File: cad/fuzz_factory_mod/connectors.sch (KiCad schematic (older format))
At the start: 21 parts, among them J1701 Barrel_Jack_Switch, J1702 Conn_Battery, J1703 CONN_AUDIO_IN, J1704 CONN_AUDIO_OUT, J2801 CONN_AUDIO_OUT_REF, J2802 CONN_EXP_1, J2803 CONN_EXP_2, K1701 EE2-5NU, Q1701 DTC114Y, Q1702 DTA114E

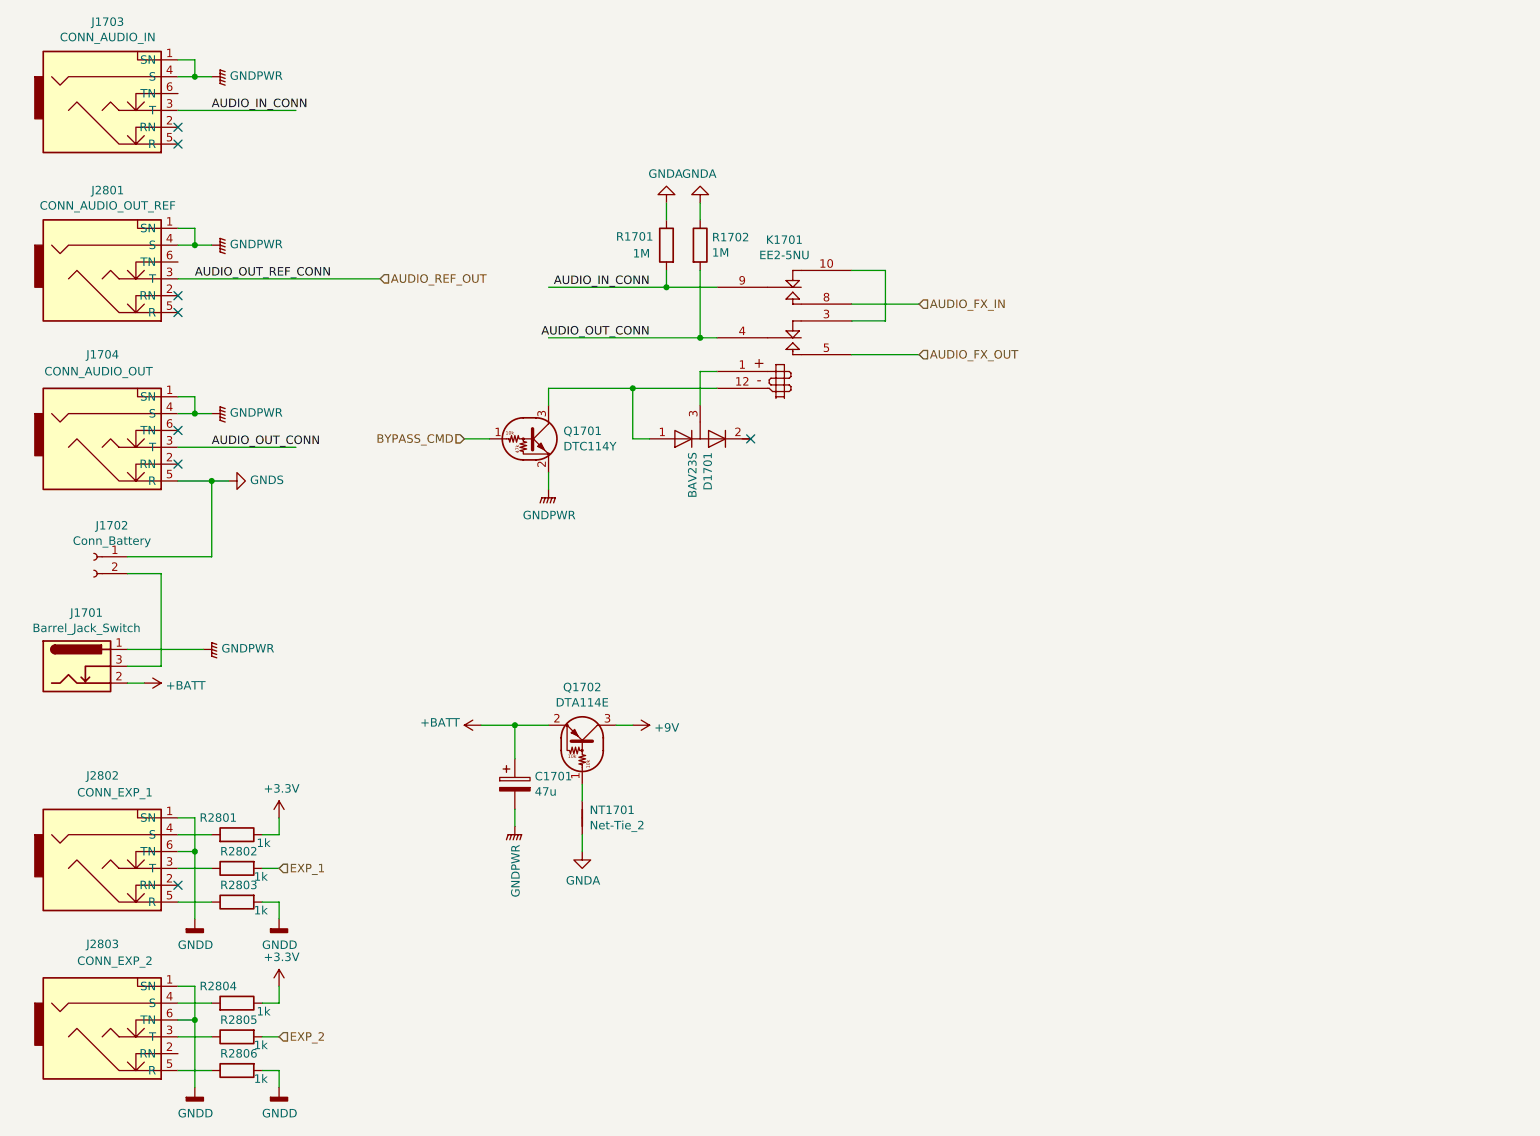
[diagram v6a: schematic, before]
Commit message: Changes architecture.
Corrections on schematic.
Continued Layout placement.
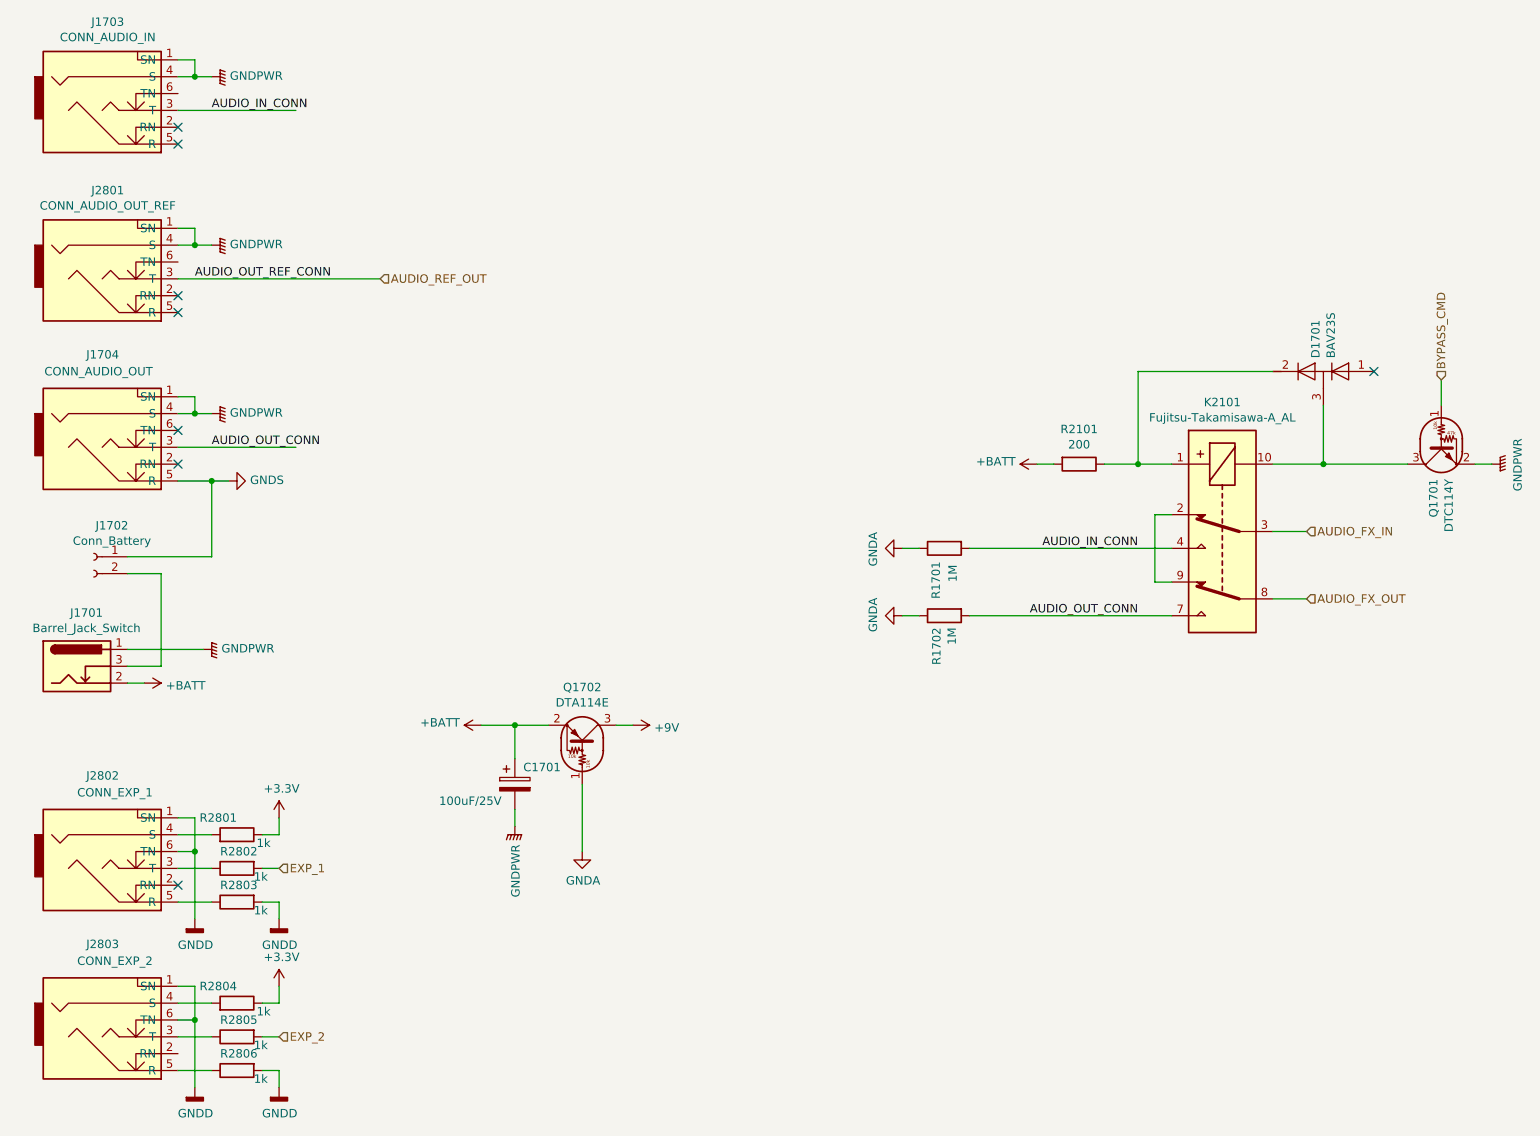
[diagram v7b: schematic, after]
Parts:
- removed K1701: EE2-5NU, flax_lib:RELAY-EE2, symbol flax_lib:EE2-5NU
- removed NT1701: Net-Tie_2, Oddities:NetTie-II, symbol Device:Net-Tie_2
- added K2101: Fujitsu-Takamisawa-A_AL, Relays_ThroughHole:Relay_DPDT_FRT5, symbol flax_lib:Fujitsu-Takamisawa-A_AL
- added R2101: 200, Resistors_SMD:R_0805, symbol Device:R
- C1701: value 47u -> 100uF/25V
- J1703, J1704, J2801, J2802, J2803: footprint Connect:NMJ6HCD2 -> flax_lib:CLIFF_FCR5005x
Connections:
- wire segments 77 -> 73
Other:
- moved on the sheet: D1701, Q1701, R1701, R1702
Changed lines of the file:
@@
 $Descr A4 11693 8268
 encoding utf-8
-Sheet 29 30
+Sheet 21 22
 Title ""
 Date ""
@@
 $EndDescr
 $Comp
-L flax_lib:EE2-5NU K1701
-U 1 1 5DE5A46A
-P 6400 2650
-F 0 "K1701" H 6400 3181 50  0000 C CNN
-F 1 "EE2-5NU" H 6400 3090 50  0000 C CNN
-F 2 "flax_lib:RELAY-EE2" H 6400 2650 50  0001 C CNN
-F 3 "" H 6400 2650 50  0000 C CNN
-	1    6400 2650
-	1    0    0    -1
-$EndComp
-$Comp
 L flax_lib:CLIFF_FCR50051 J1703
 U 1 1 5DE5BD43
@@
 F 0 "J1703" H 2383 1875 50  0000 C CNN
 F 1 "CONN_AUDIO_IN" H 2383 1784 50  0000 C CNN
-F 2 "Connect:NMJ6HCD2" H 2500 1200 50  0001 C CNN
+F 2 "flax_lib:CLIFF_FCR5005x" H 2500 1200 50  0001 C CNN
 F 3 "" H 2500 1200 50  0001 C CNN
 	1    2400 1350
@@
 F 0 "J1704" H 2450 3900 50  0000 R CNN
 F 1 "CONN_AUDIO_OUT" H 2650 3800 50  0000 R CNN
-F 2 "Connect:NMJ6HCD2" H 2500 3200 50  0001 C CNN
+F 2 "flax_lib:CLIFF_FCR5005x" H 2500 3200 50  0001 C CNN
 F 3 "" H 2500 3200 50  0001 C CNN
 	1    2400 3350
@@
 L Transistor_BJT:DTC114Y Q1701
 U 1 1 5DE5E2B7
-P 4900 3300
-F 0 "Q1701" H 5088 3346 50  0000 L CNN
-F 1 "DTC114Y" H 5088 3255 50  0000 L CNN
-F 2 "TO_SOT_Packages_SMD:SOT-23" H 4900 3300 50  0001 L CNN
-F 3 "" H 4900 3300 50  0001 L CNN
-	1    4900 3300
-	1    0    0    -1
+P 10300 3350
+F 0 "Q1701" H 10488 3396 50  0000 L CNN
+F 1 "DTC114Y" H 10488 3305 50  0000 L CNN
+F 2 "TO_SOT_Packages_SMD:SOT-23" H 10300 3350 50  0001 L CNN
+F 3 "" H 10300 3350 50  0001 L CNN
+	1    10300 3350
+	0    -1   1    0
 $EndComp
 $Comp
 L flax_lib:BAV23S D1701
 U 1 1 5DE5F68B
-P 5900 3300
-F 0 "D1701" V 5946 3379 50  0000 L CNN
-F 1 "BAV23S" V 5855 3379 50  0000 L CNN
-F 2 "TO_SOT_Packages_SMD:SOT-23" H 5900 3300 50  0001 C CNN
-F 3 "" H 5900 3300 50  0001 C CNN
-	1    5900 3300
-	1    0    0    1
+P 9600 2900
+F 0 "D1701" V 9646 2979 50  0000 L CNN
+F 1 "BAV23S" V 9555 2979 50  0000 L CNN
+F 2 "TO_SOT_Packages_SMD:SOT-23" H 9600 2900 50  0001 C CNN
+F 3 "" H 9600 2900 50  0001 C CNN
+	1    9600 2900
+	-1   0    0    -1
 $EndComp
 $Comp
@@
 	1    0    0    -1
 $EndComp
-Wire Wire Line
-	6800 2600 7000 2600
-Wire Wire Line
-	7000 2600 7000 2300
-Wire Wire Line
-	7000 2300 6800 2300
 $Comp
 L power:GNDPWR #PWR01706
 U 1 1 5E049671
-P 5000 3600
-F 0 "#PWR01706" H 5000 3400 50  0001 C CNN
-F 1 "GNDPWR" H 5004 3446 50  0000 C CNN
-F 2 "" H 5000 3550 50  0001 C CNN
-F 3 "" H 5000 3550 50  0001 C CNN
-	1    5000 3600
-	1    0    0    -1
-$EndComp
-Wire Wire Line
-	5000 3500 5000 3600
-Wire Wire Line
-	5000 3000 5000 3100
-Wire Wire Line
-	5000 3000 5500 3000
-Wire Wire Line
-	6000 2900 5900 2900
-Wire Wire Line
-	5900 2900 5900 3100
-Wire Wire Line
-	5600 3300 5500 3300
-Wire Wire Line
-	5500 3300 5500 3000
-Connection ~ 5500 3000
-Wire Wire Line
-	5500 3000 6000 3000
-NoConn ~ 6200 3300
-Text HLabel 4500 3300 0    50   Input ~ 0
+P 10600 3450
+F 0 "#PWR01706" H 10600 3250 50  0001 C CNN
+F 1 "GNDPWR" H 10604 3296 50  0000 C CNN
+F 2 "" H 10600 3400 50  0001 C CNN
+F 3 "" H 10600 3400 50  0001 C CNN
+	1    10600 3450
+	0    -1   1    0
+$EndComp
+Wire Wire Line
+	10500 3450 10600 3450
+Text HLabel 10300 2950 1    50   Input ~ 0
 BYPASS_CMD
 Wire Wire Line
-	4650 3300 4500 3300
+	10300 3100 10300 2950
 $Comp
 L Device:R R1702
 U 1 1 5E0563EF
-P 5900 2150
-F 0 "R1702" H 5970 2196 50  0000 L CNN
-F 1 "1M" H 5970 2105 50  0000 L CNN
-F 2 "Resistors_SMD:R_0603" V 5830 2150 50  0001 C CNN
-F 3 "~" H 5900 2150 50  0001 C CNN
-	1    5900 2150
-	1    0    0    -1
+P 7350 4350
+F 0 "R1702" H 7420 4396 50  0000 L CNN
+F 1 "1M" H 7420 4305 50  0000 L CNN
+F 2 "Resistors_SMD:R_0603" V 7280 4350 50  0001 C CNN
+F 3 "~" H 7350 4350 50  0001 C CNN
+	1    7350 4350
+	0    -1   1    0
 $EndComp
 $Comp
 L Device:R R1701
 U 1 1 5E056DB3
-P 5700 2150
-F 0 "R1701" H 6000 2200 50  0000 R CNN
-F 1 "1M" H 5900 2100 50  0000 R CNN
-F 2 "Resistors_SMD:R_0603" V 5630 2150 50  0001 C CNN
-F 3 "~" H 5700 2150 50  0001 C CNN
-	1    5700 2150
-	-1   0    0    -1
-$EndComp
-Wire Wire Line
-	5900 2300 5900 2700
-Connection ~ 5900 2700
-Wire Wire Line
-	5900 2700 6000 2700
-Wire Wire Line
-	5700 2300 5700 2400
-Connection ~ 5700 2400
-Wire Wire Line
-	5700 2400 6000 2400
+P 7350 3950
+F 0 "R1701" H 7650 4000 50  0000 R CNN
+F 1 "1M" H 7550 3900 50  0000 R CNN
+F 2 "Resistors_SMD:R_0603" V 7280 3950 50  0001 C CNN
+F 3 "~" H 7350 3950 50  0001 C CNN
+	1    7350 3950
+	0    -1   1    0
+$EndComp
 $Comp
 L power:GNDA #PWR01710
 U 1 1 5E058766
-P 5900 1900
-F 0 "#PWR01710" H 5900 1650 50  0001 C CNN
-F 1 "GNDA" H 5905 1727 50  0000 C CNN
-F 2 "" H 5900 1900 50  0001 C CNN
-F 3 "" H 5900 1900 50  0001 C CNN
-	1    5900 1900
-	-1   0    0    1
+P 7100 4350
+F 0 "#PWR01710" H 7100 4100 50  0001 C CNN
+F 1 "GNDA" H 7105 4177 50  0000 C CNN
+F 2 "" H 7100 4350 50  0001 C CNN
+F 3 "" H 7100 4350 50  0001 C CNN
+	1    7100 4350
+	0    1    -1   0
 $EndComp
 $Comp
 L power:GNDA #PWR01709
 U 1 1 5E059243
-P 5700 1900
-F 0 "#PWR01709" H 5700 1650 50  0001 C CNN
-F 1 "GNDA" H 5705 1727 50  0000 C CNN
-F 2 "" H 5700 1900 50  0001 C CNN
-F 3 "" H 5700 1900 50  0001 C CNN
-	1    5700 1900
-	-1   0    0    1
-$EndComp
-Wire Wire Line
-	5900 1900 5900 2000
-Wire Wire Line
-	5700 1900 5700 2000
-Text HLabel 7200 2500 2    50   Input ~ 0
+P 7100 3950
+F 0 "#PWR01709" H 7100 3700 50  0001 C CNN
+F 1 "GNDA" H 7105 3777 50  0000 C CNN
+F 2 "" H 7100 3950 50  0001 C CNN
+F 3 "" H 7100 3950 50  0001 C CNN
+	1    7100 3950
+	0    1    1    0
+$EndComp
+Wire Wire Line
+	7100 4350 7200 4350
+Wire Wire Line
+	7100 3950 7200 3950
+Text HLabel 9500 3850 2    50   Input ~ 0
 AUDIO_FX_IN
-Text HLabel 7200 2800 2    50   Input ~ 0
+Text HLabel 9500 4250 2    50   Input ~ 0
 AUDIO_FX_OUT
-Wire Wire Line
-	7200 2800 6800 2800
-Wire Wire Line
-	6800 2500 7200 2500
 Wire Wire Line
 	2600 4750 2500 4750
@@
 NoConn ~ 2800 1450
 NoConn ~ 2800 1550
-Text Label 5600 2400 2    50   ~ 0
+Text Label 8500 3950 2    50   ~ 0
 AUDIO_IN_CONN
-Text Label 5600 2700 2    50   ~ 0
+Text Label 8500 4350 2    50   ~ 0
 AUDIO_OUT_CONN
-Wire Wire Line
-	5000 2700 5900 2700
-Wire Wire Line
-	5000 2400 5700 2400
 $Comp
 L Transistor_BJT:DTA114E Q1702
@@
 	0    1    -1   0
 $EndComp
-$Comp
-L Device:CP C1701
-U 1 1 5E6D0A71
-P 4800 5350
-F 0 "C1701" H 4918 5396 50  0000 L CNN
-F 1 "47u" H 4918 5305 50  0000 L CNN
-F 2 "Capacitors_SMD:CP_Elec_6.3x4.5" H 4838 5200 50  0001 C CNN
-F 3 "~" H 4800 5350 50  0001 C CNN
-	1    4800 5350
-	1    0    0    -1
-$EndComp
 Wire Wire Line
 	5000 5000 4800 5000
@@
 	5500 5000 5400 5000
 $Comp
-L Device:Net-Tie_2 NT1701
-U 1 1 5E6DBA2F
-P 5200 5550
-F 0 "NT1701" V 5154 5594 50  0000 L CNN
-F 1 "Net-Tie_2" V 5245 5594 50  0000 L CNN
-F 2 "Oddities:NetTie-II" H 5200 5550 50  0001 C CNN
-F 3 "~" H 5200 5550 50  0001 C CNN
-	1    5200 5550
-	0    1    1    0
-$EndComp
-Wire Wire Line
-	5200 5350 5200 5450
-Wire Wire Line
-	5200 5650 5200 5750
-$Comp
 L flax_lib:CLIFF_FCR50051 J2802
 U 1 1 5ECDD75B
@@
 F 0 "J2802" H 2450 6400 50  0000 R CNN
 F 1 "CONN_EXP_1" H 2650 6300 50  0000 R CNN
-F 2 "Connect:NMJ6HCD2" H 2500 5700 50  0001 C CNN
+F 2 "flax_lib:CLIFF_FCR5005x" H 2500 5700 50  0001 C CNN
 F 3 "" H 2500 5700 50  0001 C CNN
 	1    2400 5850
@@
 F 0 "J2803" H 2450 7400 50  0000 R CNN
 F 1 "CONN_EXP_2" H 2650 7300 50  0000 R CNN
-F 2 "Connect:NMJ6HCD2" H 2500 6700 50  0001 C CNN
+F 2 "flax_lib:CLIFF_FCR5005x" H 2500 6700 50  0001 C CNN
 F 3 "" H 2500 6700 50  0001 C CNN
 	1    2400 6850
@@
 F 0 "J2801" H 2383 2875 50  0000 C CNN
 F 1 "CONN_AUDIO_OUT_REF" H 2383 2784 50  0000 C CNN
-F 2 "Connect:NMJ6HCD2" H 2500 2200 50  0001 C CNN
+F 2 "flax_lib:CLIFF_FCR5005x" H 2500 2200 50  0001 C CNN
 F 3 "" H 2500 2200 50  0001 C CNN
 	1    2400 2350
@@
 Wire Wire Line
 	2800 2350 4000 2350
+$Comp
+L flax_lib:Fujitsu-Takamisawa-A_AL K2101
+U 1 1 5EFDB4D3
+P 9000 3850
+F 0 "K2101" V 8233 3850 50  0000 C CNN
+F 1 "Fujitsu-Takamisawa-A_AL" V 8324 3850 50  0000 C CNN
+F 2 "Relays_ThroughHole:Relay_DPDT_FRT5" H 9650 3800 50  0001 L CNN
+F 3 "http://omronfs.omron.com/en_US/ecb/products/pdf/en-g6k.pdf" H 8800 3850 50  0001 C CNN
+	1    9000 3850
+	0    -1   1    0
+$EndComp
+Wire Wire Line
+	8700 4150 8600 4150
+Wire Wire Line
+	8600 4150 8600 3750
+Wire Wire Line
+	8600 3750 8700 3750
+$Comp
+L Device:R R2101
+U 1 1 5EFEC6A7
+P 8150 3450
+F 0 "R2101" V 7943 3450 50  0000 C CNN
+F 1 "200" V 8034 3450 50  0000 C CNN
+F 2 "Resistors_SMD:R_0805" V 8080 3450 50  0001 C CNN
+F 3 "~" H 8150 3450 50  0001 C CNN
+	1    8150 3450
+	0    1    1    0
+$EndComp
+$Comp
+L power:+BATT #PWR0125
+U 1 1 5EFEDA1A
+P 7900 3450
+F 0 "#PWR0125" H 7900 3300 50  0001 C CNN
+F 1 "+BATT" V 7915 3577 50  0000 L CNN
+F 2 "" H 7900 3450 50  0001 C CNN
+F 3 "" H 7900 3450 50  0001 C CNN
+	1    7900 3450
+	0    -1   -1   0
+$EndComp
+Wire Wire Line
+	8000 3450 7900 3450
+NoConn ~ 9900 2900
+Wire Wire Line
+	7500 3950 8700 3950
+Wire Wire Line
+	7500 4350 8700 4350
+Wire Wire Line
+	9300 3850 9500 3850
+Wire Wire Line
+	9500 4250 9300 4250
+Wire Wire Line
+	9300 3450 9600 3450
+Wire Wire Line
+	8300 3450 8500 3450
+Wire Wire Line
+	9600 3100 9600 3450
+Connection ~ 9600 3450
+Wire Wire Line
+	9600 3450 10100 3450
+Wire Wire Line
+	9300 2900 8500 2900
+Wire Wire Line
+	8500 2900 8500 3450
+Connection ~ 8500 3450
+Wire Wire Line
+	8500 3450 8700 3450
+$Comp
+L Device:CP C?
+U 1 1 5F12F439
+P 4800 5350
+AR Path="/5E2FAB43/5F12F439" Ref="C?"  Part="1"
+AR Path="/5DE5A177/5F12F439" Ref="C1701"  Part="1"
+F 0 "C1701" H 4850 5450 50  0000 L CNN
+F 1 "100uF/25V" H 4350 5250 50  0000 L CNN
+F 2 "Capacitors_SMD:CP_Elec_6.3x4.5" H 4838 5200 50  0001 C CNN
+F 3 "~" H 4800 5350 50  0001 C CNN
+	1    4800 5350
+	1    0    0    -1
+$EndComp
+Wire Wire Line
+	5200 5350 5200 5750
 $EndSCHEMATC
